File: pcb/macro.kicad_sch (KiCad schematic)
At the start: 17 parts, among them K1 KEYSW, K2 KEYSW, K3 KEYSW, K4 KEYSW, K5 KEYSW, K6 KEYSW, U1 ProMicro

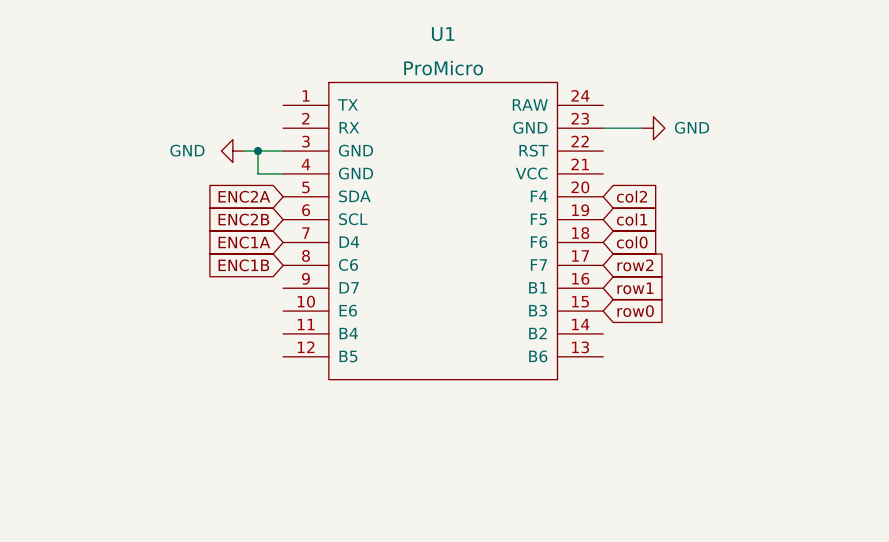
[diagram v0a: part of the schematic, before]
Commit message: feat: add button switch for reset
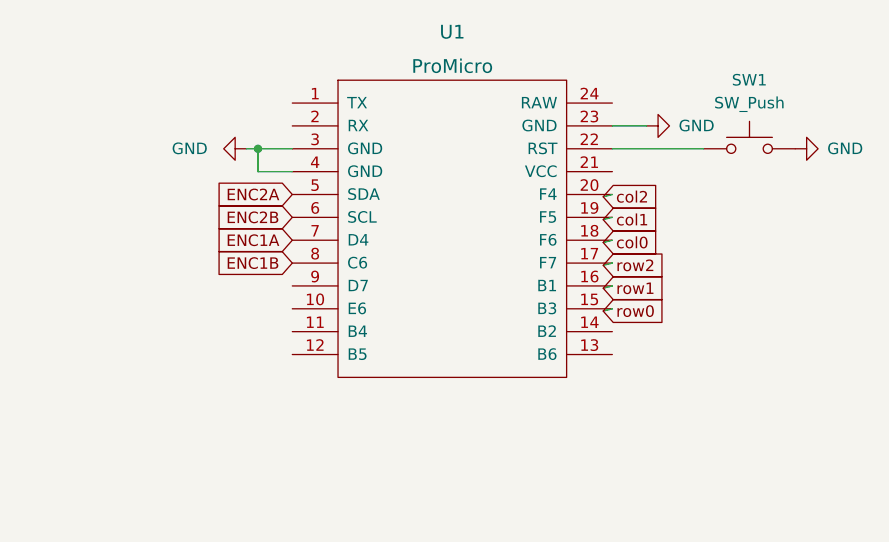
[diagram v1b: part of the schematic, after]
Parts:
- added SW1: SW_Push, Button_Switch_SMD:SW_SPST_CK_RS282G05A3, symbol Switch:SW_Push
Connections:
- net GND: now also SW1.2
- net at U1.22 (RST): now also SW1.1
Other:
- moved on the sheet: U1
